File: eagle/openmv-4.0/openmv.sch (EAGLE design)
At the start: 42 parts, among them U1 OV9650, U2 USD-47571, U3 ADP322, U4 STM32F407LQFP100, U5 BEAD, X1 USB-MICROB, Y2 RESONATORSMD

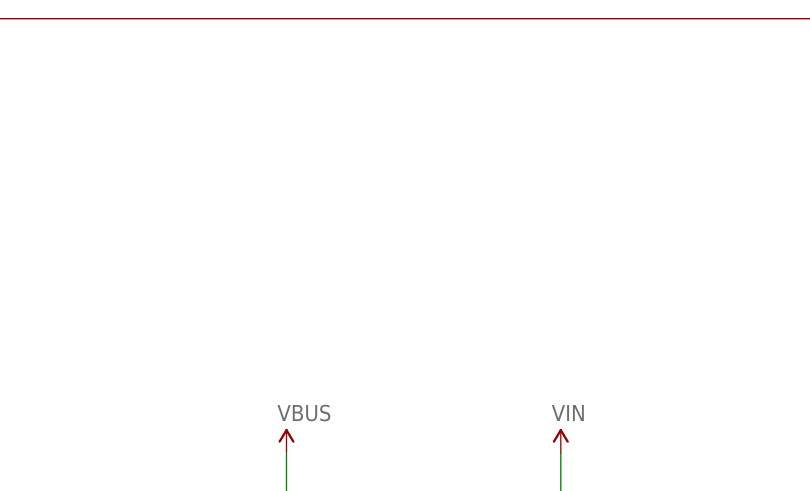
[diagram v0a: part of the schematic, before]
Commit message: Update REV4
* Add regulator test points
* Remove 10mil via
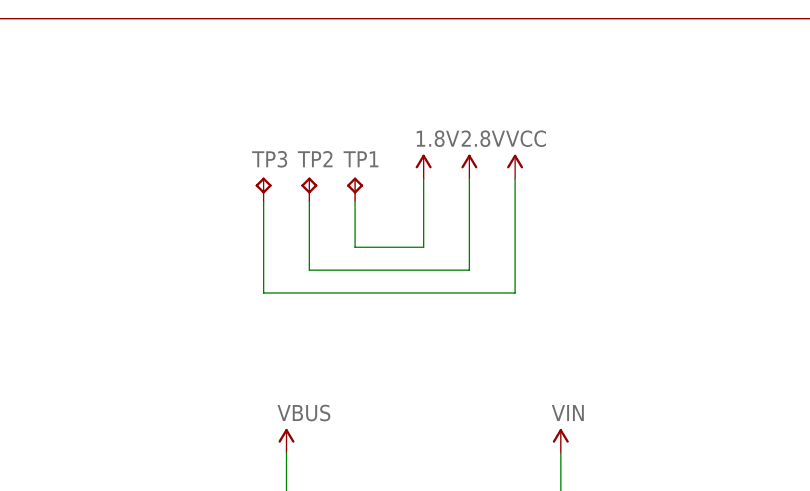
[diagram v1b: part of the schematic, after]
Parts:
- added TP1, TP2, TP3: TPTP10R, testpad:TPTP10R
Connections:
- net 1.8V: now also TP1.TP
- net 2.8V: now also TP2.TP
- net VCC: now also TP3.TP
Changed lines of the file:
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@@
 <part name="Y2" library="sfe" deviceset="RESONATOR" device="SMD"/>
 <part name="LED2" library="adafruit" deviceset="RGBLED" device="5050"/>
+<part name="TP2" library="testpad" deviceset="TP" device="TP10R"/>
+<part name="TP1" library="testpad" deviceset="TP" device="TP10R"/>
+<part name="U$3" library="sfe" deviceset="2.8V" device=""/>
+<part name="U$4" library="sfe" deviceset="1.8V" device=""/>
+<part name="TP3" library="testpad" deviceset="TP" device="TP10R">
+<attribute name="TP_SIGNAL_NAME" value=""/>
+</part>
+<part name="P+1" library="SparkFun" deviceset="VCC" device=""/>
 </parts>
 <sheets>
@@
 </instance>
 <instance part="LED2" gate="G$1" x="149.86" y="10.16" rot="R180"/>
+<instance part="TP2" gate="G$1" x="160.02" y="154.94"/>
+<instance part="TP1" gate="G$1" x="165.1" y="154.94"/>
+<instance part="U$3" gate="G$1" x="177.8" y="154.94"/>
+<instance part="U$4" gate="G$1" x="172.72" y="154.94"/>
+<instance part="TP3" gate="G$1" x="154.94" y="154.94"/>
+<instance part="P+1" gate="1" x="182.88" y="154.94"/>
 </instances>
 <busses>
@@
 <pinref part="U$1" gate="G$1" pin="2.8V"/>
 </segment>
+<segment>
+<pinref part="TP2" gate="G$1" pin="TP"/>
+<wire x1="160.02" y1="152.4" x2="160.02" y2="144.78" width="0.1524" layer="91"/>
+<wire x1="160.02" y1="144.78" x2="177.8" y2="144.78" width="0.1524" layer="91"/>
+<wire x1="177.8" y1="144.78" x2="177.8" y2="154.94" width="0.1524" layer="91"/>
+<pinref part="U$3" gate="G$1" pin="2.8V"/>
+</segment>
 </net>
 <net name="BOOT0" class="0">
@@
 <pinref part="U$12" gate="G$1" pin="1.8V"/>
 <pinref part="U1" gate="G$1" pin="DVDD"/>
+</segment>
+<segment>
+<pinref part="TP1" gate="G$1" pin="TP"/>
+<wire x1="165.1" y1="152.4" x2="165.1" y2="147.32" width="0.1524" layer="91"/>
+<wire x1="165.1" y1="147.32" x2="172.72" y2="147.32" width="0.1524" layer="91"/>
+<wire x1="172.72" y1="147.32" x2="172.72" y2="154.94" width="0.1524" layer="91"/>
+<pinref part="U$4" gate="G$1" pin="1.8V"/>
 </segment>
 </net>
@@
 <junction x="177.8" y="7.62"/>
 </segment>
-</net>
+<segment>
+<pinref part="TP3" gate="G$1" pin="TP"/>
+<wire x1="154.94" y1="152.4" x2="154.94" y2="142.24" width="0.1524" layer="91"/>
+<wire x1="154.94" y1="142.24" x2="182.88" y2="142.24" width="0.1524" layer="91"/>
+<wire x1="182.88" y1="142.24" x2="182.88" y2="154.94" width="0.1524" layer="91"/>
+<pinref part="P+1" gate="1" pin="VCC"/>
+</segment>
+</net>

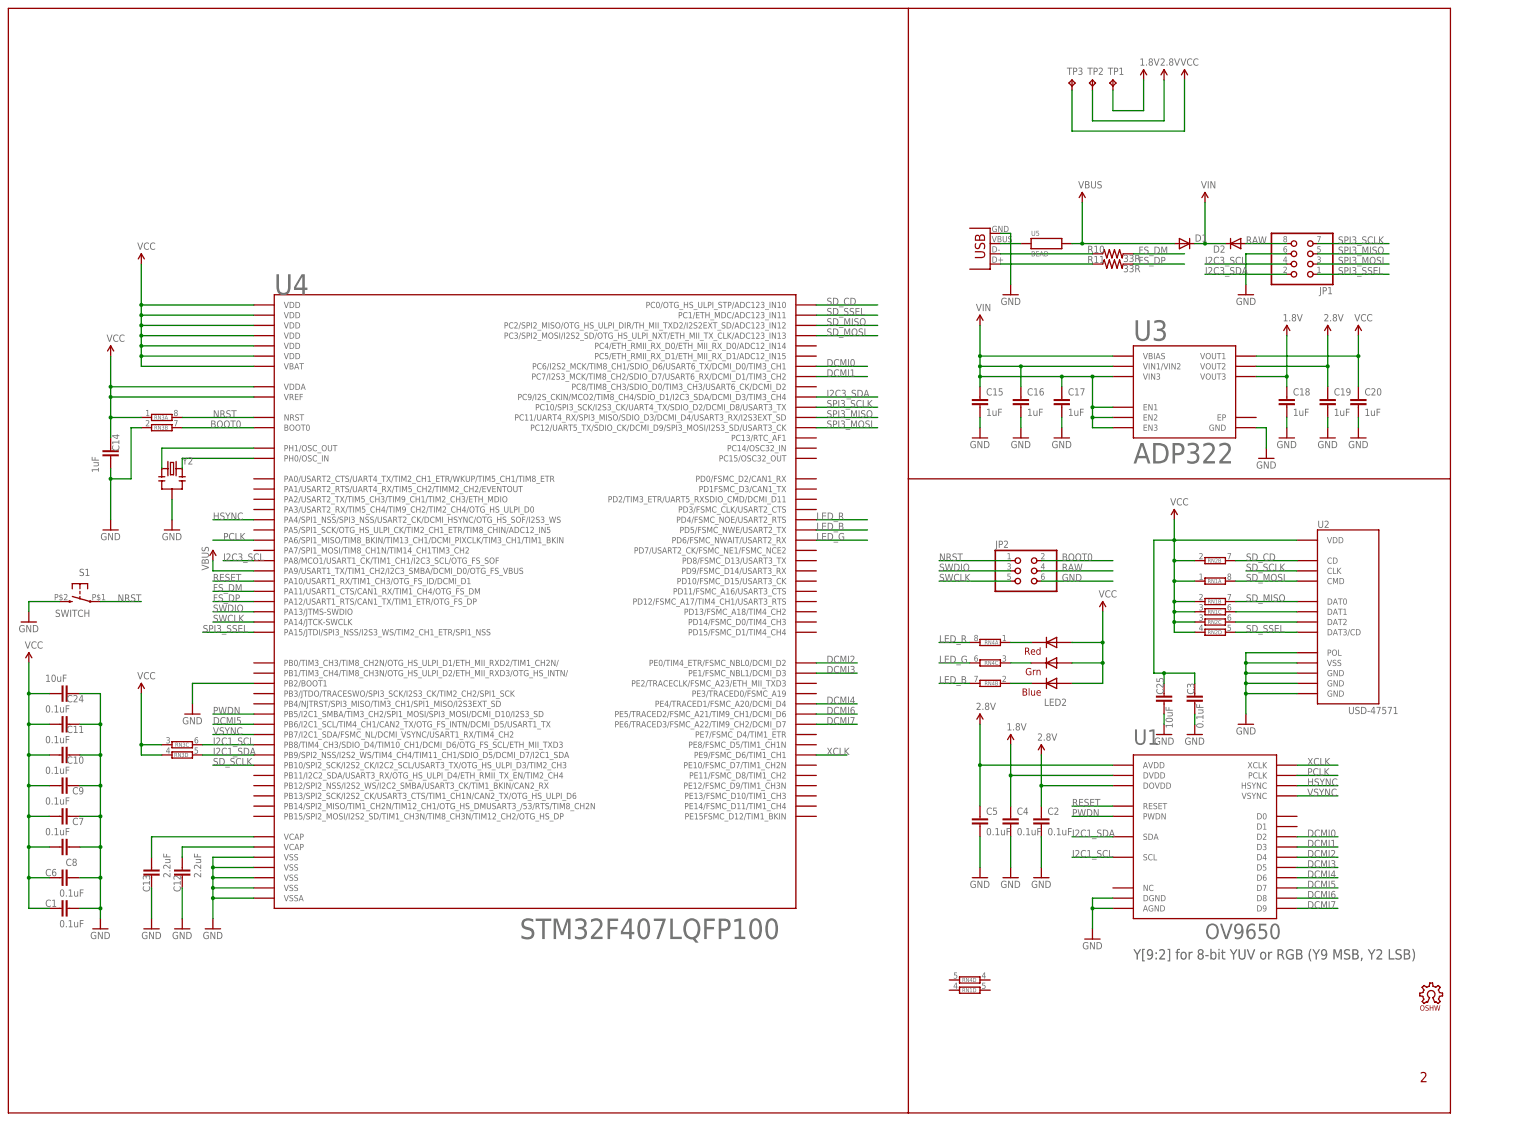
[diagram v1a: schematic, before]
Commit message: Update REV4
* Use a different I2C multiplexed with USART
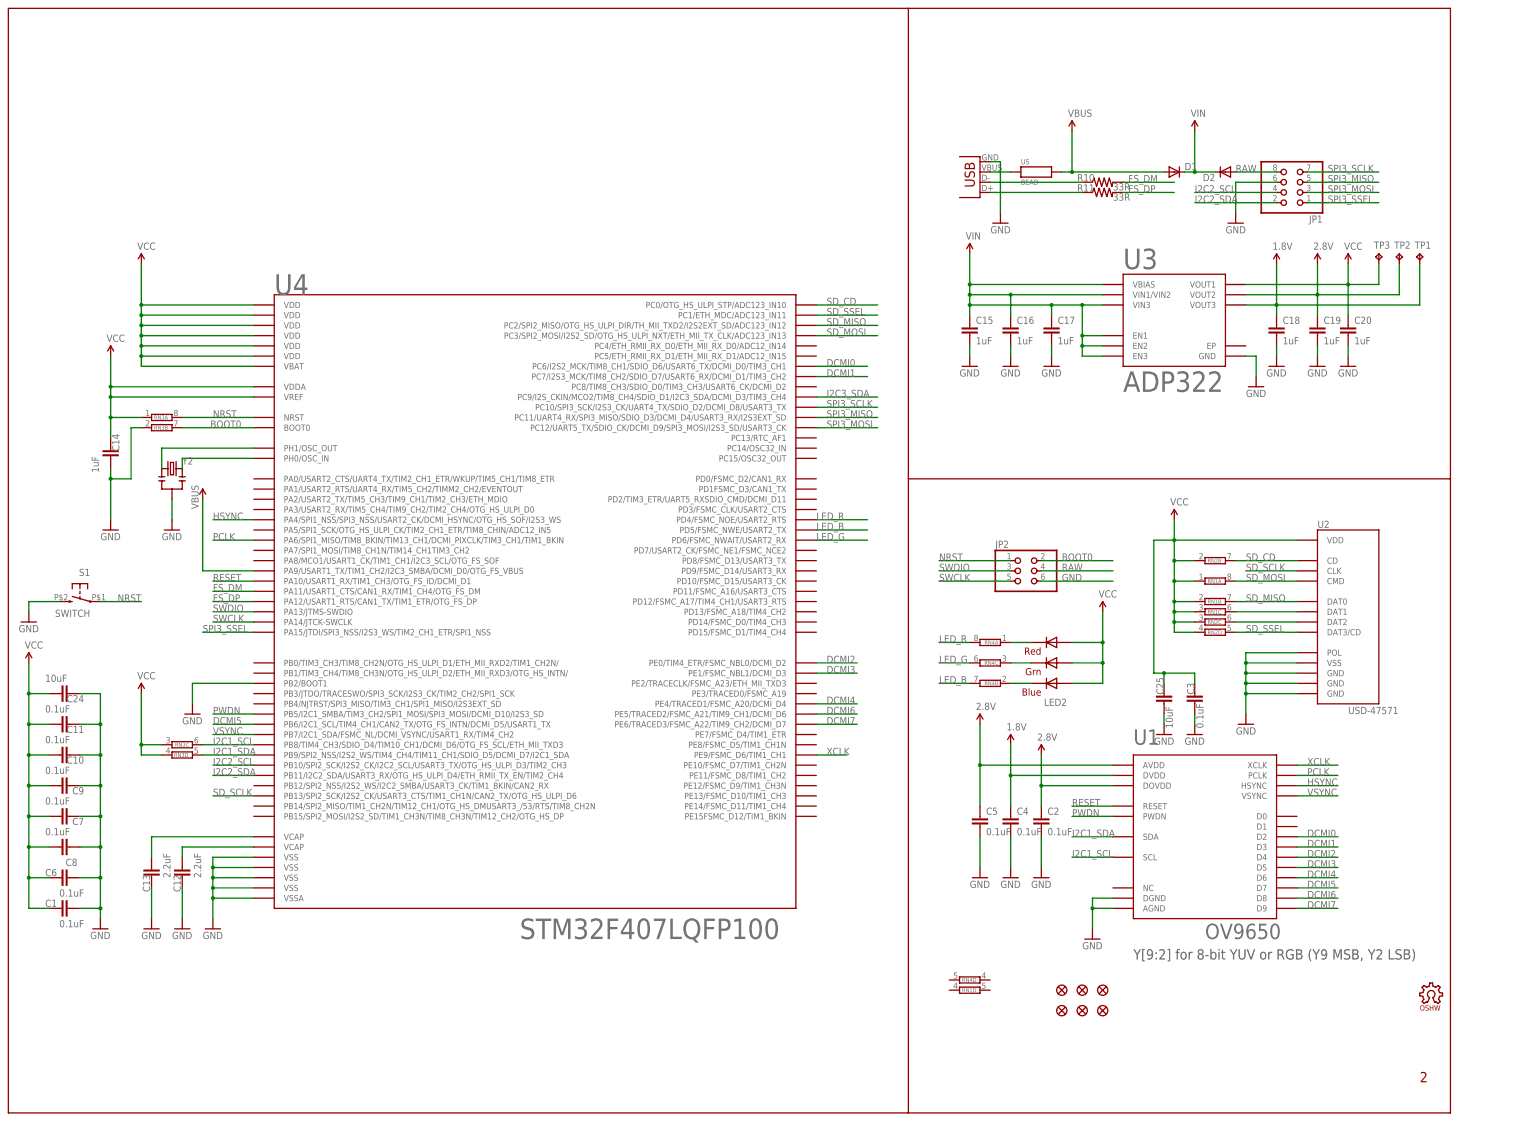
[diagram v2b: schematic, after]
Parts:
- added JP3, JP4, JP5, JP6, JP7, JP8: FIDUCIAL1X2, sfe:FIDUCIAL1X2
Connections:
- removed net I2C3_SCL: JP1.4, U4.PA8/MCO1/USART1_CK/TIM1_CH1/I2C3_SCL/OTG_FS_SOF
- new net I2C2_SCL: JP1.4, U4.PB10/SPI2_SCK/I2S2_CK/I2C2_SCL/USART3_TX/OTG_HS_ULPI_D3/TIM2_CH3
- new net I2C2_SDA: JP1.2, U4.PB11/I2C2_SDA/USART3_RX/OTG_HS_ULPI_D4/ETH_RMII_TX_EN/TIM2_CH4
- net I2C3_SDA: no longer JP1.2
- net SD_SCLK: now also U4.PB13/SPI2_SCK/I2S2_CK/USART3_CTS/TIM1_CH1N/CAN2_TX/OTG_HS_ULPI_D6; no longer U4.PB10/SPI2_SCK/I2S2_CK/I2C2_SCL/USART3_TX/OTG_HS_ULPI_D3/TIM2_CH3
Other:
- moved on the sheet: C15, C16, C17, C18, C19, C20, D1, D2, JP1, R10, R11, TP1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

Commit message: Update HW REV4
* Use dual LDO
* Add I2C EEPROM
* Update RESET switch
* Add bulk cap to STM VCC
* Add diode on debug VCC
* Add bead for sensor filter
* Use separate USART
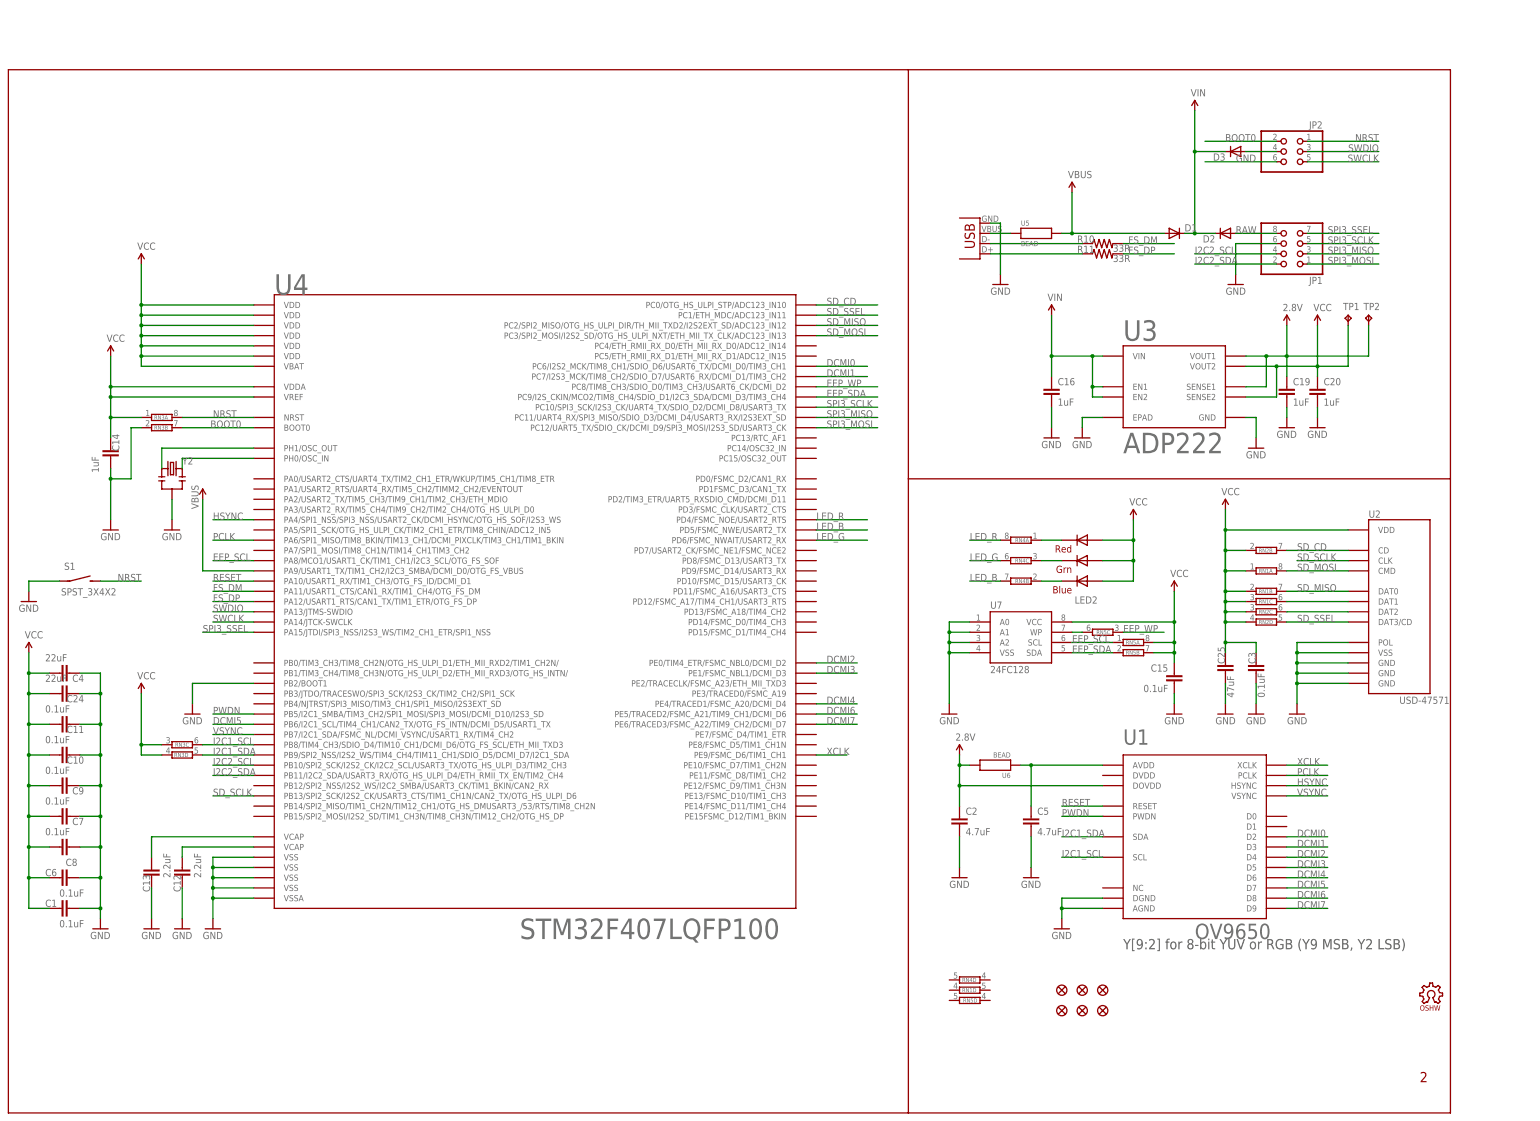
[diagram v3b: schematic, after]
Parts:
- removed C17, C18: 1uF, sfe:CAP0402-CAP
- removed TP3: TPTP10R, testpad:TPTP10R
- added D3: (no value), sfe:DIODESOD
- added RN5: (no value), resistor-dil:4R-NCAT16
- added U6: BEAD, heka:BEAD
- added U7: 24FC128, mux:24FC128
- C15: value 1uF -> 0.1uF
- C2, C5: value 0.1uF -> 4.7uF
- C24: value 10uF -> 22uF
- C25: value 10uF -> 47uF
- C4: value 0.1uF -> 22uF; device sfe:CAP0402-CAP -> sfe:CAP0805
- S1: value SWITCH -> SPST_3X4X2; device mux:SWITCH -> bt_electromech:SPST_3X4X2
- U3: value ADP322 -> ADP222; device iofault:ADP322 -> mux:ADP222
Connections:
- removed net 1.8V: C18.1, C4.1, TP1.TP, U1.DVDD, U3G$1.VOUT3
- removed net I2C3_SDA: U4.PC9/I2S_CKIN/MCO2/TIM8_CH4/SDIO_D1/I2C3_SDA/DCMI_D3/TIM3_CH4
- new net EEP_SCL: RN5A.1, U4.PA8/MCO1/USART1_CK/TIM1_CH1/I2C3_SCL/OTG_FS_SOF, U7.SCL
- new net EEP_SDA: RN5B.1, U4.PC9/I2S_CKIN/MCO2/TIM8_CH4/SDIO_D1/I2C3_SDA/DCMI_D3/TIM3_CH4, U7.SDA
- new net EEP_WP: RN5C.1, U4.PC8/TIM8_CH3/SDIO_D0/TIM3_CH3/USART6_CK/DCMI_D2
- new net N$10: C5.1, U1.AVDD, U6.1
- new net N$11: D3.A, JP2.4
- new net N$9: RN5C.2, U7.WP
- net 2.8V: now also U3.SENSE1, U3.VOUT1, U6.2; no longer C5.1, U1.AVDD, U3G$1.VOUT2
- net GND: now also C4.1, S1.P, U3.EPAD, U3.GND, U7.A0, U7.A1, U7.A2, U7.VSS; no longer C17.2, C18.2, C4.2, S1.2, U3G$1.GND
- net NRST: now also S1.S; no longer S1.1
- net RAW: no longer JP2.4
- net SPI3_MISO: now also JP1.3; no longer JP1.5
- net SPI3_MOSI: now also JP1.1; no longer JP1.3
- net SPI3_SCLK: now also JP1.5; no longer JP1.7
- net SPI3_SSEL: now also JP1.7; no longer JP1.1
- net VCC: now also C15.1, C4.2, RN5A.2, RN5B.2, TP1.TP, U3.SENSE2, U3.VOUT2, U7.VCC; no longer TP3.TP, U3G$1.VOUT1
- net VIN: now also D3.C, U3.EN1, U3.EN2, U3.VIN; no longer C15.1, C17.1, U3G$1.EN1, U3G$1.EN2, U3G$1.EN3, U3G$1.VBIAS, U3G$1.VIN1/VIN2, U3G$1.VIN3
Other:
- note added: "Debug Header"
- moved on the sheet: C15, C16, C19, C2, C20, C25, C3, C4, C5, D1, D2, JP1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
